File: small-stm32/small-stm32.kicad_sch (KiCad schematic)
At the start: 41 parts, among them J1 USB_C_Receptacle, J3 QWIIC, U2 STM32G0B1CBUxN, Y1 8Mhz SMD2520-4P

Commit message: update-2025-12-08
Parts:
- U3: value ~ -> SGM6029; footprint Package_CSP:WLCSP-6_1.4x1.0mm_P0.4mm -> seeed-stuff:WLCSP-0.74×1.09-6B
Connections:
- net MODE: now reaches R9.2, U3.C1 (MODE)
- net SW: now reaches L1.1, U3.B2 (SW)
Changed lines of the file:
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@@
 	)
 	(junction
+		(at 57.15 132.08)
+		(diameter 0)
+		(color 0 0 0 0)
+	)
+	(junction
 		(at 48.26 99.06)
 		(diameter 0)
@@
 	(wire
 		(pts
+			(xy 57.15 125.73) (xy 57.15 132.08)
+		)
+		(stroke
+			(width 0)
+			(type default)
+		)
+	)
+	(wire
+		(pts
 			(xy 48.26 99.06) (xy 48.26 101.6)
 		)
@@
 	(wire
 		(pts
+			(xy 57.15 132.08) (xy 58.42 132.08)
+		)
+		(stroke
+			(width 0)
+			(type default)
+		)
+	)
+	(wire
+		(pts
 			(xy 228.6 129.54) (xy 231.14 129.54)
 		)
@@
 	(wire
 		(pts
-			(xy 55.88 132.08) (xy 58.42 132.08)
+			(xy 55.88 132.08) (xy 57.15 132.08)
 		)
 		(stroke
@@
 		)
 	)
+	(label "SW"
+		(at 57.15 125.73 0)
+		(effects
+			(font
+				(size 1.27 1.27)
+			)
+			(justify left bottom)
+		)
+	)
 	(label "4"
 		(at 85.09 60.96 180)
@@
 		)
 	)
+	(label "MODE"
+		(at 57.15 137.16 0)
+		(effects
+			(font
+				(size 1.27 1.27)
+			)
+			(justify left bottom)
+		)
+	)
 	(global_label "D-"
 		(shape input)
@@
 			)
 		)
-		(property "Value" "~"
+		(property "Value" "SGM6029"
 			(at 48.26 127 0)
 			(effects
@@
 			)
 		)
-		(property "Footprint" "Package_CSP:WLCSP-6_1.4x1.0mm_P0.4mm"
+		(property "Footprint" "seeed-stuff:WLCSP-0.74×1.09-6B"
 			(at 48.26 125.73 0)
 			(effects

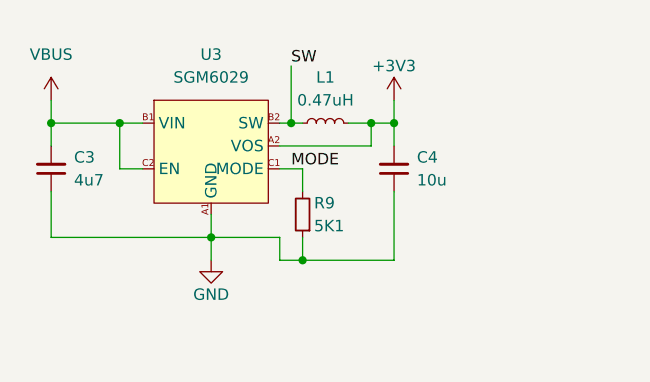
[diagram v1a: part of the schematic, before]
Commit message: bump to KiCAD 10
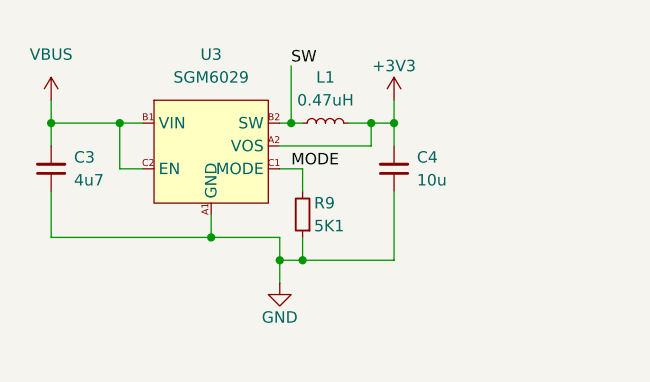
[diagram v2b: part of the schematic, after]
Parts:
- U1: value ~ -> (none)
